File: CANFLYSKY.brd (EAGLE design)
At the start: 100 x 60 mm, 47 parts, among them J1 USB_B_PTH, SW1 SWITCH-DPDT3, U1 MCP2551, X1 INPUT, X2 OUTPUT

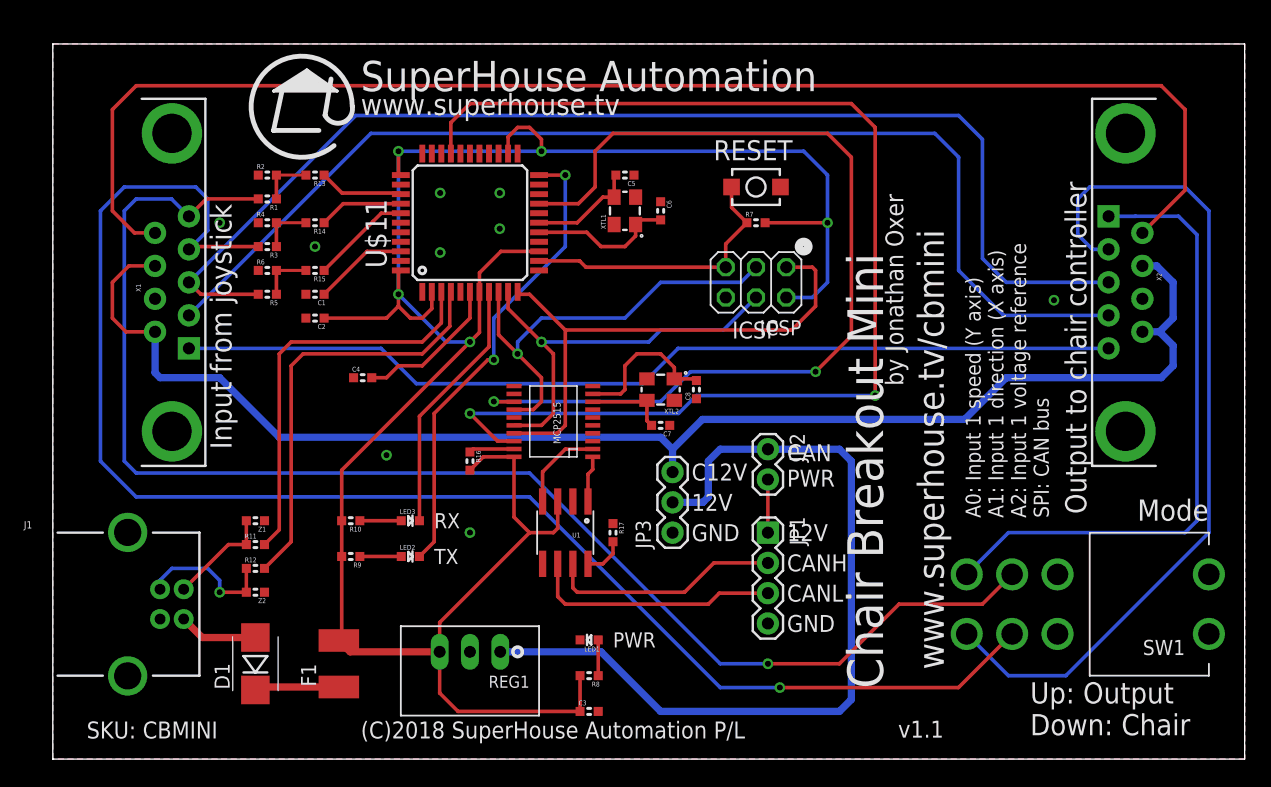
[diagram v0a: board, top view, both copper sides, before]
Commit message: Removed unnecessary parts
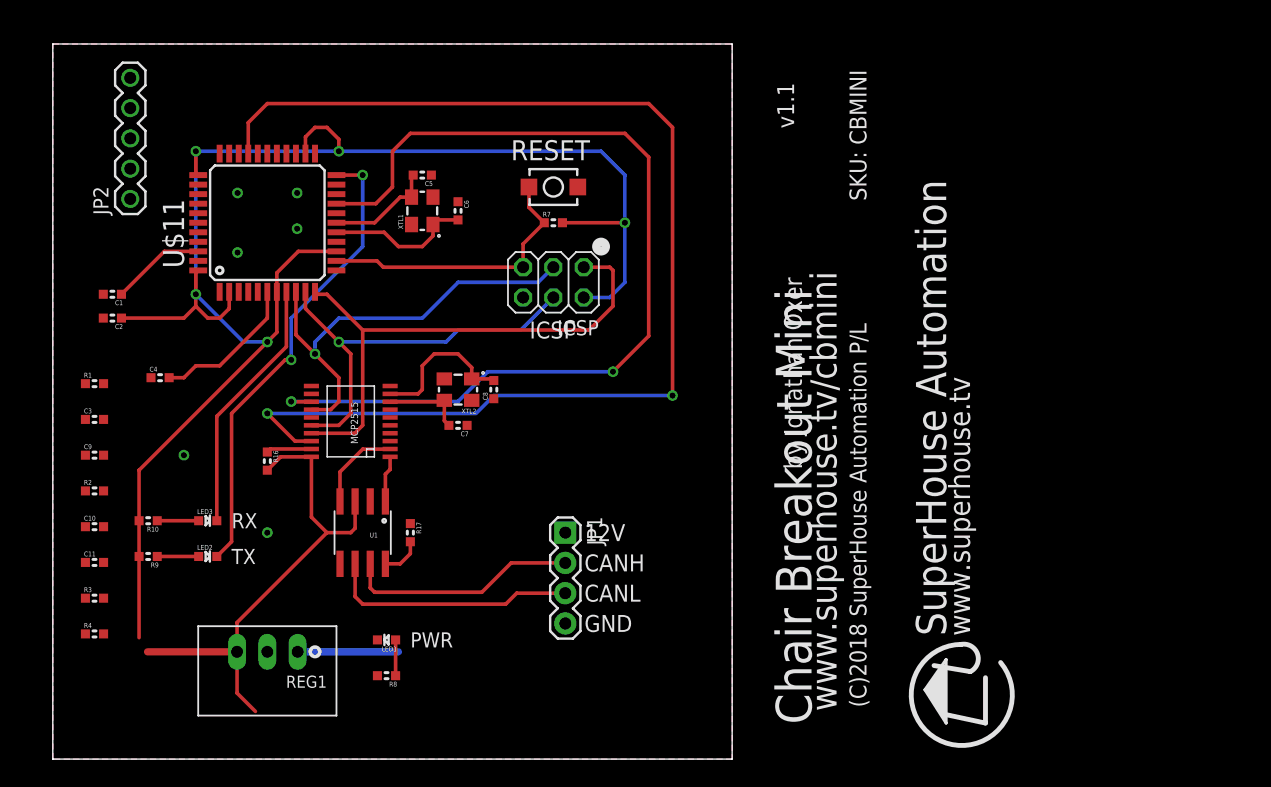
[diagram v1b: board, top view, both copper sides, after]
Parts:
- removed D1: 1N4004, freetronics-jon:SMB-DIODE
- removed F1: 500mA PTC 1812, rcl:L1812
- removed J1: USB_B_PTH, SparkFun-Connectors:USB-B-PTH
- removed JP3: PWR, freetronics-jon:1X03
- removed R11, R12: 22R, freetronics-jon:0603
- removed R13, R14, R15: 1K, freetronics-jon:0603
- removed R5, R6: 47K 1%, freetronics-jon:0603
- removed SW1: SWITCH-DPDT3, freetronics-jon:7201SD9AV2BE
- removed X1: INPUT, SparkFun-Connectors:DB9_MALE
- removed X2: OUTPUT, SparkFun-Connectors:DB9
- removed Z1, Z2: PGB1010603, freetronics-master-v1.1:0603
- added C10, C11, C9: 1uF, freetronics-master-v1.1:0603
- JP2: value PWR -> (none); device freetronics-jon:1X02 -> freetronics-jon:1X05
- R1, R2, R3, R4: value 47K 1% -> 4K7; device freetronics-jon:0603 -> freetronics-master-v1.1:0603
- moved JP2 57.5 mm to (6.50, 47.0), turned to 90 degrees
- moved C3 48.2 mm to (3.50, 28.5)
- moved R4 37.4 mm to (3.50, 10.5)
- moved R3 32.9 mm to (3.50, 13.5), turned to 0 degrees
- moved R2 30.2 mm to (3.50, 22.5)
- moved R1 21.2 mm to (3.50, 31.5), turned to 0 degrees
- moved C1 17.0 mm to (5.00, 39.0)
- moved C2 17.0 mm to (5.00, 37.0)
- moved C4 17.0 mm to (9.00, 32.0)
- moved C5 17.0 mm to (31.0, 49.0)
- moved C6 17.0 mm to (34.0, 46.0)
- moved C7 17.0 mm to (34.0, 28.0)
- moved C8 17.0 mm to (37.0, 31.0)
- moved ICSP 17.0 mm to (42.0, 40.0)
- moved JP1 17.0 mm to (43.0, 19.0)
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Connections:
- removed net C12V: JP3.3, X1.7, X1.9, X2.7, X2.9
- removed net D+: J1.D+, R12.1, Z2.2
- removed net D-: J1.D-, R11.1, Z1.2
- removed net DETECT: X1.5, X2.5
- removed net DIRECTION_IN: R3.2, SW1.5, X1.2
- removed net DIRECTION_OUT: SW1.4, X2.2
- removed net N$1: X1.6, X2.6
- removed net N$15: JP1.1, JP2.2
- removed net N$17: D1.C, F1.1
- removed net N$2: R1.1, R13.2, R2.2
- removed net N$3: R14.2, R3.1, R4.2
- removed net N$4: R15.2, R5.1, R6.2
- removed net N$6: X1.4, X2.4
- removed net RD+: R12.2, U$11.4
- removed net RD-: R11.2, U$11.3
- removed net REFERENCE: R5.2, X1.3, X2.3
- removed net SPEED_IN: R1.2, SW1.2, X1.1
- removed net SPEED_OUT: SW1.3, X2.1
- removed net USB+: D1.A, J1.VBUS
- new net OUT_X1: C3.1, JP2.1, R1.2
- new net OUT_X2: C10.1, JP2.3, R3.2
- new net OUT_Y1: C9.1, JP2.2, R2.2
- new net OUT_Y2: C11.1, JP2.4, R4.2
- net 12V: now also JP1.1; no longer JP2.1, JP3.2
- net 5V: no longer C3.1, F1.2
- net A0: no longer R13.1
- net A1: no longer R14.1
- net A2: no longer R15.1
- net D3_SCL: now also R1.1
- net D5: now also R2.1
- net D6_A8: now also R3.1
- net D9_A10: now also R4.1
- net GND: now also C10.2, C11.2, C9.2, JP2.5; no longer J1.GND, J1.SHLD1, J1.SHLD2, JP3.1, R2.1, R4.1, R6.1, X1.8, X2.8, Z1.1, Z2.1
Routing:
- net DIRECTION_IN: track 128.3 -> 0.00 mm, vias 1 -> 0
- net C12V: track 120.3 -> 0.00 mm
- net SPEED_IN: track 118.5 -> 0.00 mm, vias 1 -> 0
- net N$1: track 116.3 -> 0.00 mm
- net REFERENCE: track 100.8 -> 0.00 mm
- net N$6: track 95.4 -> 0.00 mm
- net DETECT: track 79.6 -> 0.00 mm
- net DIRECTION_OUT: track 72.1 -> 0.00 mm
- net 12V: track 71.0 -> 8.46 mm
- net SPEED_OUT: track 53.2 -> 0.00 mm
- net RD+: track 35.5 -> 0.00 mm
- net RD-: track 33.8 -> 0.00 mm
- net 5V: track 195.6 -> 180.7 mm
- net D+: track 11.8 -> 0.00 mm, vias 1 -> 0
- net D-: track 8.81 -> 0.00 mm
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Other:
- board size 100 x 60 mm -> 57 x 60 mm
- board text removed: "A0: Input 1 speed (Y axis) A1: Input 1 direction (X axis) A2: Input 1 voltage reference SPI: CAN bus"
- board text removed: "C12V"
- board text removed: "CAN PWR"
- board text removed: "Input from joystick"
- board text removed: "Mode"
- board text removed: "Output to chair controller"
- board text removed: "Up: Output Down: Chair"

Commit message: Completed initial routing
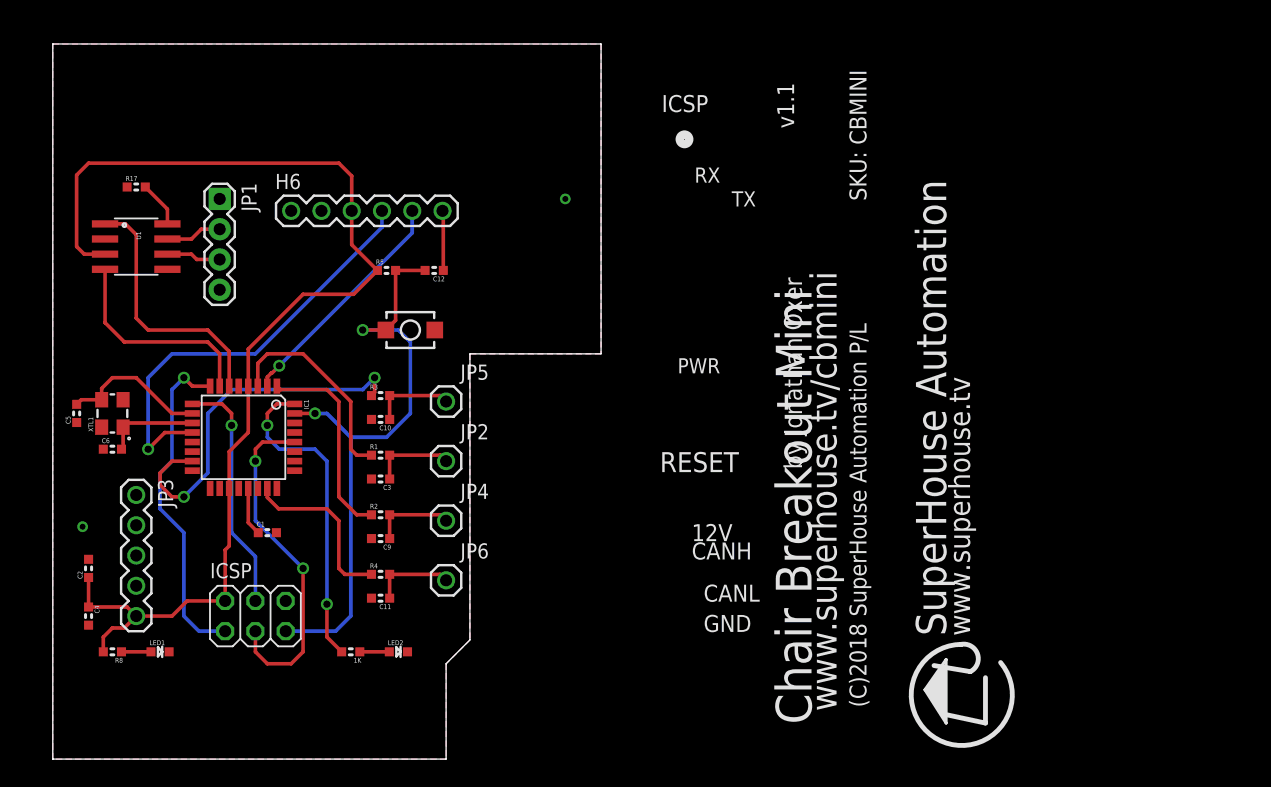
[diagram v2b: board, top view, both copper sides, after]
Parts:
- removed C7, C8: 15pF, freetronics-master-v1.1:0603
- removed LED3: GREEN, freetronics-jon:LED-0603
- removed R10, R9: 1K, freetronics-jon:0603
- removed R16, R7: 10K, freetronics-master-v1.1:0603
- removed REG1: K7805-500R3, freetronics-jon:K78XX-500R3
- removed U$11: ATMEGA32U4NT, freetronics-jon:TQFP44
- removed U$4: MCP2515, MCP2515:TSSOP20
- removed XTL2: 16MHz, freetronics-jon:CRYSTAL-SMD-3X2
- added 1K: 1K, freetronics-jon:0603
- added C12: 100nF, freetronics-master-v1.1:0603
- added H6: USB-TTL, freetronics:1X06
- added IC1: ATMEGA32M1, freetronics-jon:TQFP32-08
- added JP3: (no value), freetronics-jon:1X05
- added JP4, JP5, JP6: M01PTH, freetronics-jon:1X01
- added R5: 10K, freetronics-master-v1.1:0603
- JP2: value (none) -> M01PTH; device freetronics-jon:1X05 -> freetronics-jon:1X01
- XTL1: value 16MHz -> 8MHz
- moved JP1 40.3 mm to (14.0, 47.0)
- moved ICSP 37.5 mm to (17.0, 12.0), turned to 0 degrees
- moved R17 37.0 mm to (7.00, 48.0), turned to 0 degrees
- moved C5 35.2 mm to (2.00, 29.0), turned to 90 degrees
- moved C6 35.2 mm to (5.00, 26.0), turned to 0 degrees
- moved JP2 34.4 mm to (33.0, 25.0), turned to 0 degrees
- moved XTL1 31.1 mm to (5.00, 29.0)
- moved U1 30.6 mm to (7.00, 43.0), turned to 270 degrees
- moved R3 29.4 mm to (27.5, 30.5)
- moved C10 25.6 mm to (27.5, 28.5), turned to 180 degrees
- moved C9 25.0 mm to (27.5, 18.5), turned to 180 degrees
- moved R1 24.7 mm to (27.5, 25.5)
- moved C3 24.5 mm to (27.5, 23.5), turned to 180 degrees
- moved R4 24.5 mm to (27.5, 15.5)
- moved C11 24.2 mm to (27.5, 13.5), turned to 180 degrees
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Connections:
- removed net 3V3: C4.2, U$11.6
- removed net 5V: C2.1, ICSP.2, R10.2, R16.2, R7.2, R8.2, R9.2, REG1.3, U$11.14, U$11.2, U$11.24, U$11.34, U$11.44, U$11.7, U$4.20, U1.3
- removed net D0: U$11.20
- removed net D1: U$11.21
- removed net D10_A11: U$11.30, U$4.18
- removed net D2_SDA: U$11.19, U$4.13
- removed net D3_SCL: R1.1, U$11.18
- removed net D4_A6: U$11.25
- removed net D5: R2.1, U$11.31
- removed net D6_A8: R3.1, U$11.27
- removed net D7_AIN0: U$11.1
- removed net D8_A9: U$11.28
- removed net D9_A10: R4.1, U$11.29
- removed net HWB: U$11.33
- removed net MISO: ICSP.1, U$11.11, U$4.17
- removed net MOSI: ICSP.4, U$11.10, U$4.16
- removed net N$10: R16.1, U$4.19
- removed net N$13: U$4.2, U1.4
- removed net N$14: C8.2, U$4.9, XTL2.1
- removed net N$18: C7.2, U$4.8, XTL2.3
- removed net N$7: LED2.A, R9.1
- removed net N$8: LED3.A, R10.1
- removed net N$9: U$4.1, U1.1
- removed net RXLED_SS: LED3.C, U$11.8
- removed net TX_LED: LED2.C, U$11.22
- new net 3.3V: C2.1, C4.1, H6.3, IC1.19, IC1.4, ICSP.2, JP3.5, R5.1, R8.2, U1.3
- new net A6: IC1.26
- new net A7: IC1.27
- new net D0_RX: H6.4, IC1.12
- new net D10: IC1.25
- new net D14: IC1.1, R2.1
- new net D1_TX: H6.5, IC1.2
- new net D2: IC1.3, R1.1
- new net D3_TXCAN: IC1.6, U1.1
- new net D4_RXCAN: IC1.7, U1.4
- new net D5_MISO: IC1.8, ICSP.1
- new net D6_MOSI: IC1.9, ICSP.4
- new net D7: IC1.15, R3.1
- new net D8: IC1.23, R4.1
- new net D9: IC1.24
- new net FS_RESET: JP3.1
- new net FS_SWD_CLK: JP3.4
- new net FS_SWD_DIO: JP3.3
- new net N$1: 1K.1, LED2.A
- new net RTS: C12.1, H6.6
- net 12V: no longer REG1.1
- net A0: now also IC1.13; no longer U$11.36
- net A1: now also IC1.14; no longer U$11.37
- net A2: now also IC1.16; no longer U$11.38
- net A3: now also IC1.17; no longer U$11.39
- net A4: now also IC1.18; no longer U$11.40
- net A5: now also IC1.22; no longer U$11.41
- net AREF: now also IC1.21; no longer U$11.42
- net D11: now also IC1.29; no longer U$11.12
- net D12: now also IC1.30; no longer U$11.26
- net D13: now also 1K.2, IC1.32; no longer U$11.32
- net GND: now also C4.2, H6.1, H6.2, IC1.20, IC1.5, JP3.2, LED2.C; no longer C4.1, C7.1, C8.1, JP2.5, REG1.2, U$11.15, U$11.23, U$11.35, U$11.43, U$11.5, U$4.10, XTL2.2, XTL2.4
- net N$11: now also IC1.10; no longer U$11.17
- net N$12: now also IC1.11; no longer U$11.16
- net OUT_X2: now also JP5.1; no longer JP2.3
- net OUT_Y1: now also JP4.1; no longer JP2.2
- net OUT_Y2: now also JP6.1; no longer JP2.4
- net RESET: now also C12.2, IC1.31, R5.2; no longer R7.1, U$11.13
- net SCK: now also IC1.28; no longer U$11.9, U$4.14
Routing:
- net 5V: track 180.7 -> 0.00 mm, vias 5 -> 0
- net D10_A11: track 101.5 -> 0.00 mm, vias 2 -> 0
- net 3.3V: track 0.00 -> 96.4 mm
- net D2_SDA: track 80.2 -> 0.00 mm, vias 2 -> 0
- net MISO: track 45.3 -> 0.00 mm
- net TX_LED: track 39.6 -> 0.00 mm, vias 2 -> 0
- net D0_RX: track 0.00 -> 36.5 mm, vias 0 -> 1
- net MOSI: track 35.0 -> 0.00 mm, vias 1 -> 0
- net D7: track 0.00 -> 31.2 mm, vias 0 -> 2
- net RESET: track 23.9 -> 52.5 mm, vias 0 -> 2
- net D5_MISO: track 0.00 -> 28.1 mm, vias 0 -> 1
- net D13: track 0.00 -> 27.0 mm, vias 0 -> 2
- net D3_TXCAN: track 0.00 -> 21.9 mm
- net RXLED_SS: track 21.6 -> 0.00 mm
- net D6_MOSI: track 0.00 -> 20.2 mm, vias 0 -> 1
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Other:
- board size 57 x 60 mm -> 46 x 60 mm

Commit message: Finished routing
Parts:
- moved R17 7.00 mm to (7.00, 41.0)
- moved JP1 6.08 mm to (13.0, 41.0)
- moved 1K 6.00 mm to (25.0, 3.00)
- moved C1 6.00 mm to (18.0, 13.0)
- moved C10 6.00 mm to (27.5, 22.5)
- moved C11 6.00 mm to (27.5, 7.50)
- moved C2 6.00 mm to (3.00, 10.0)
- moved C3 6.00 mm to (27.5, 17.5)
- moved C4 6.00 mm to (3.00, 6.00)
- moved C5 6.00 mm to (2.00, 23.0)
- moved C6 6.00 mm to (5.00, 20.0)
- moved C9 6.00 mm to (27.5, 12.5)
- moved IC1 6.00 mm to (16.0, 21.0)
- moved ICSP 6.00 mm to (17.0, 6.00)
- moved JP2 6.00 mm to (33.0, 19.0)
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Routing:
- net 3.3V: track 96.4 -> 101.8 mm
- net D1_TX: track 19.8 -> 21.8 mm
- net D0_RX: track 36.5 -> 38.5 mm
- net RTS: track 5.03 -> 4.03 mm
- net CANL: track 4.57 -> 3.57 mm
- net CANH: track 4.73 -> 3.73 mm
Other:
- board size 46 x 60 mm -> 35 x 49 mm
- board text added: "1"
- board text added: "3.3V"
- board text added: "6"
- board text added: "Atmega32m1 8MHz 3.3V"
- board text added: "Black"
- board text added: "CTS"
- board text added: "FS-i6 CAN Interface"
- board text added: "RTS"
- board text added: "RXD"
- board text added: "Released under the TAPR Open Hardware License: tapr.org/OHL"
- board text added: "SKU: FSI6CAN"
- board text added: "TXD"
- board text added: "X1 D2"
- board text added: "X2 D7"
- board text added: "Y1 14"
- board text added: "Y2 D8"
- board text added: "by Jon Oxer"
- board text added: "v1.0"
- board text added: "www.superhouse.tv/fsi6can"
- board text removed: "Chair Breakout Mini"
- board text removed: "PWR"
- board text removed: "RX"
- board text removed: "SKU: CBMINI"
- board text removed: "TX"
- board text removed: "by Jonathan Oxer"
- board text removed: "v1.1"
- board text removed: "www.superhouse.tv"
- board text removed: "www.superhouse.tv/cbmini"
